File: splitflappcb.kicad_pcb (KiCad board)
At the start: 2 copper layers, 40 x 80 mm, 46 parts, among them J1 Conn_01x04_Pin, J2 Conn_01x04_Pin, J3 Conn_01x05_Pin, J4 AddressJumpers, J5 HallSensor, J6 AVR-ISP-6, J7 Serial-328P, J8 Serial-ESP12E, J9 WS2815, SW1 RESET, U1 TPS5430, U2 ULN2003A, U3 ATmega328P-A, U4 ESP-12E, Y2 16MHz

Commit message: how many attempts does it take
me when i try to use git
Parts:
- removed the REF** at (74.5, 111.3)
- removed the REF** at (82.9, 111.4)
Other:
- board text added: "Split-Flap PCB Erzerum's Mod"
- board text added: "rev 1.2b"
- board text removed: "Split-Flap Fae PCB"
- board text removed: "rev 1.2"

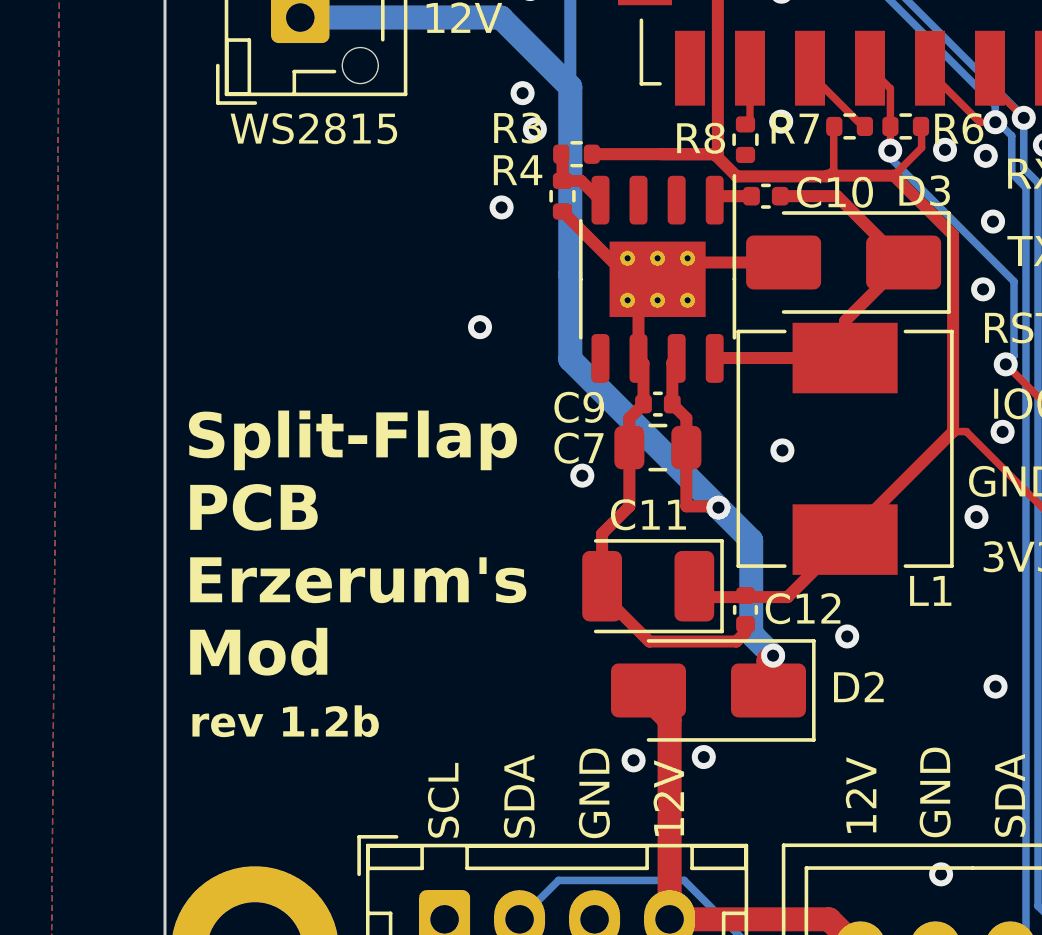
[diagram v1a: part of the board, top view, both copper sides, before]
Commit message: Changed out a tantalum capacitor for four better ones
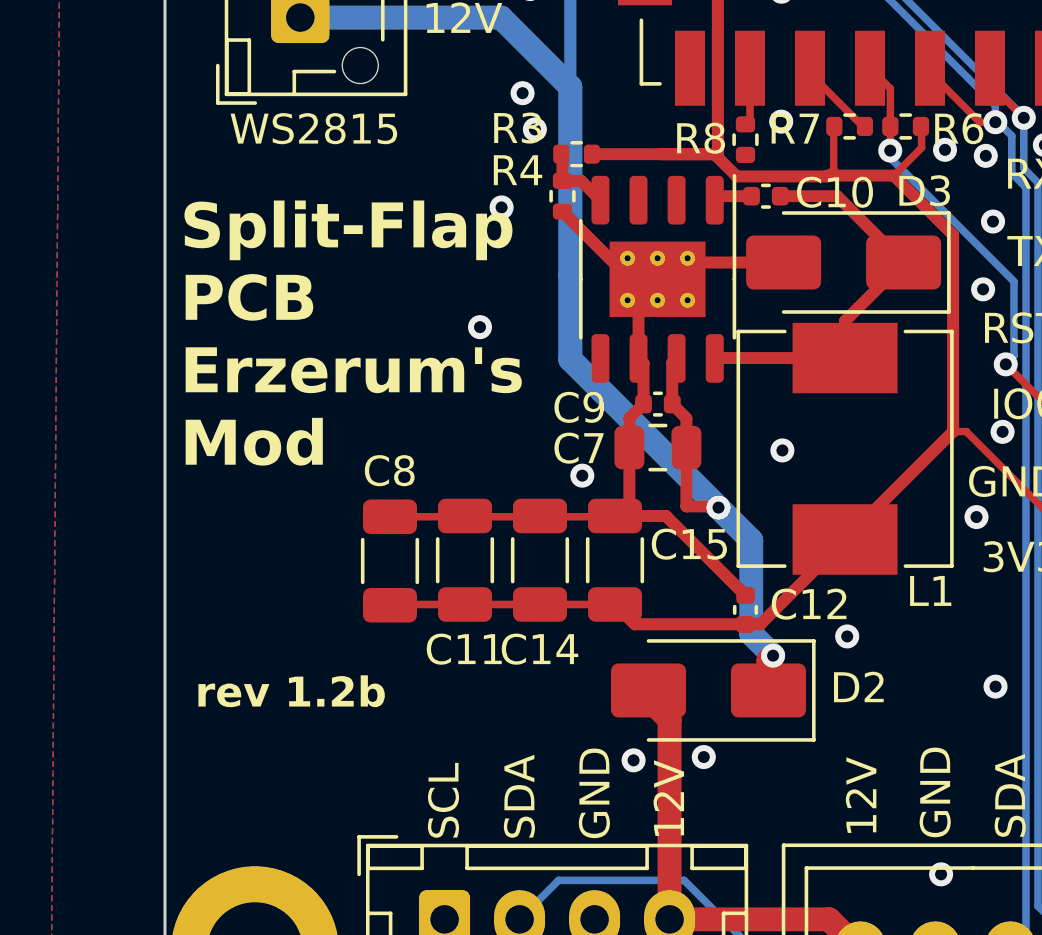
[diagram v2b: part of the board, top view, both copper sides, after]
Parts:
- added C14: 100u, Capacitor_SMD:C_1206_3216Metric, F.Cu at (79.5, 111.0)
- added C15: 100u, Capacitor_SMD:C_1206_3216Metric, F.Cu at (82.0, 111.0)
- added C8: 100u, Capacitor_SMD:C_1206_3216Metric, F.Cu at (74.5, 111.0)
- C11: value 220uF -> 100u; footprint Capacitor_Tantalum_SMD:CP_EIA-3528-21_Kemet-B -> Capacitor_SMD:C_1206_3216Metric
- moved C11 6.17 mm to (77.0, 111.0), turned to 90 degrees
- turned C12 to 90 degrees
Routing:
- net +3V3: track 141.7 -> 152.1 mm
- net GND: track 36.6 -> 41.2 mm

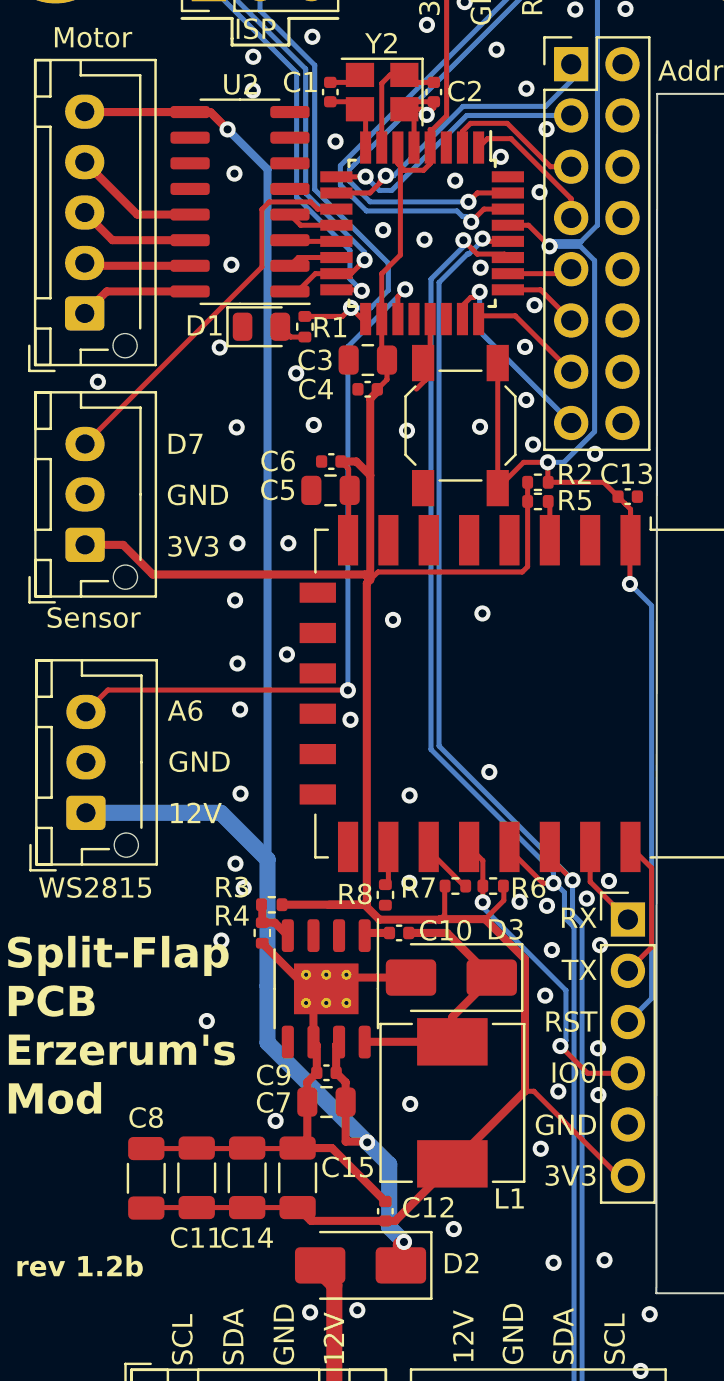
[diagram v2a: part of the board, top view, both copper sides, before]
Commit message: Fixed several drc errors
also slightly adjusted some of the silkscreen
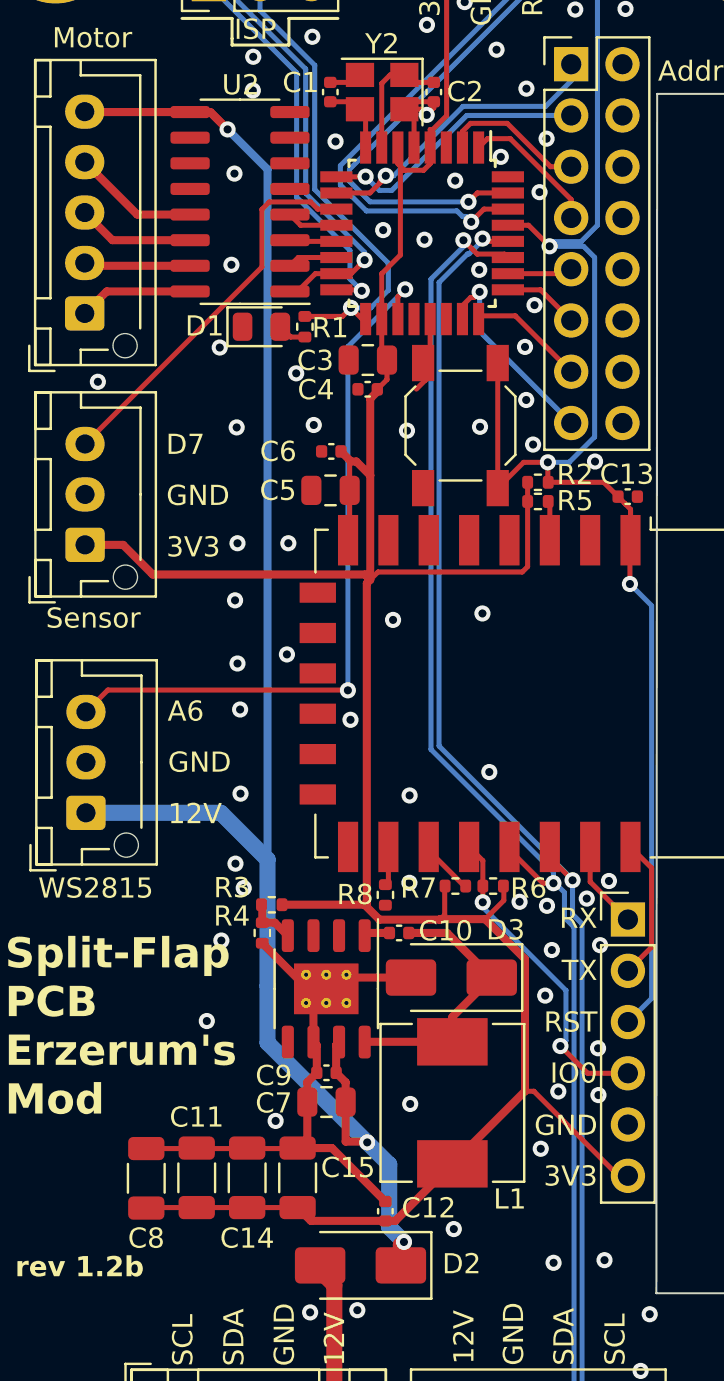
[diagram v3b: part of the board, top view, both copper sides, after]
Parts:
- moved C6 0.50 mm to (83.7, 75.0)
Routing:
- net +3V3: track 152.1 -> 151.1 mm
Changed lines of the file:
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@@
 		(tags "capacitor")
 		(property "Reference" "C8"
-			(at 2.975 0 0)
+			(at -2.975 0 0)
 			(layer "F.SilkS")
 			(effects
@@
 	(footprint "Capacitor_SMD:C_0402_1005Metric"
 		(layer "F.Cu")
-		(at 83.67 75.5)
+		(at 83.67 75)
 		(descr "Capacitor SMD 0402 (1005 Metric), square (rectangular) end terminal, IPC_7351 nominal, (Body size source: IPC-SM-782 page 76, https://www.pcb-3d.com/wordpress/wp-content/uploads/ipc-sm-782a_amendment_1_and_2.pdf), generated with kicad-footprint-generator")
 		(tags "capacitor")
@@
 		(tags "capacitor")
 		(property "Reference" "C11"
-			(at -3 0 0)
+			(at 3 0 0)
 			(layer "F.SilkS")
 			(effects
@@
 	)
 	(segment
+		(start 84.58 79.32)
+		(end 84.58 76.93)
+		(width 0.25)
+		(layer "F.Cu")
+		(net 4)
+	)
+	(segment
 		(start 85.6 81.36)
 		(end 85.6 76.19)
@@
 	)
 	(segment
-		(start 84.53 75.88)
-		(end 84.53 79.37)
-		(width 0.25)
+		(start 84.65 75.5)
+		(end 84.15 75)
+		(width 0.4)
 		(layer "F.Cu")
 		(net 4)
 	)
 	(segment
-		(start 84.18 75.53)
-		(end 84.53 75.88)
-		(width 0.25)
+		(start 85.6 81.36)
+		(end 85.43 81.53)
+		(width 0.4)
 		(layer "F.Cu")
 		(net 4)
@@
 	)
 	(segment
-		(start 85.43 81.53)
-		(end 85.6 81.36)
-		(width 0.4)
+		(start 84.58 76.93)
+		(end 84.58 75.43)
+		(width 0.25)
 		(layer "F.Cu")
 		(net 4)
 	)
 	(segment
-		(start 83.53 97.465)
-		(end 85.43 97.465)
-		(width 0.4)
+		(start 84.5 79.4)
+		(end 84.58 79.32)
+		(width 0.25)
 		(layer "F.Cu")
 		(net 4)
@@
 	)
 	(segment
+		(start 84.58 75.43)
+		(end 84.15 75)
+		(width 0.25)
+		(layer "F.Cu")
+		(net 4)
+	)
+	(segment
 		(start 73.349924 79.63)
 		(end 71.465 79.63)
@@
 	)
 	(segment
-		(start 85.43 97.465)
-		(end 85.43 81.53)
-		(width 0.4)
-		(layer "F.Cu")
-		(net 4)
-	)
-	(segment
 		(start 85.6 81.36)
 		(end 85.985 80.975)
@@
 	)
 	(segment
-		(start 93.71 106.71)
-		(end 97.91 110.91)
-		(width 0.25)
+		(start 84.91 75.5)
+		(end 84.65 75.5)
+		(width 0.4)
 		(layer "F.Cu")
 		(net 4)
 	)
 	(segment
-		(start 84.53 79.37)
-		(end 84.5 79.4)
+		(start 93.71 106.71)
+		(end 97.91 110.91)
 		(width 0.25)
 		(layer "F.Cu")
@@
 	)
 	(segment
+		(start 85.43 81.53)
+		(end 85.43 97.465)
+		(width 0.4)
+		(layer "F.Cu")
+		(net 4)
+	)
+	(segment
 		(start 88.57 60.74)
 		(end 88.57 59.94)
@@
 	)
 	(segment
-		(start 81.23 97.465)
-		(end 85.316262 97.465)
-		(width 0.4)
-		(layer "F.Cu")
-		(net 4)
-	)
-	(segment
-		(start 84.91 75.5)
-		(end 84.15 75.5)
-		(width 0.4)
-		(layer "F.Cu")
-		(net 4)
-	)
-	(segment
 		(start 89.29 96.56)
 		(end 89.29 97.97)
@@
 	)
 	(segment
+		(start 85.43 97.465)
+		(end 81.23 97.465)
+		(width 0.4)
+		(layer "F.Cu")
+		(net 4)
+	)
+	(segment
 		(start 88.700305 59.045)
 		(end 89.385 58.360305)
@@
 	)
 	(segment
-		(start 91.41 59.5)
-		(end 90.97 59.94)
+		(start 92.54 59.5)
+		(end 91.41 59.5)
 		(width 0.25)
 		(layer "F.Cu")
@@
 	)
 	(segment
-		(start 95.56 62.48)
-		(end 92.58 59.5)
+		(start 91.41 59.5)
+		(end 90.97 59.94)
 		(width 0.25)
 		(layer "F.Cu")
@@
 	(segment
 		(start 95.56 63.43)
-		(end 95.56 62.48)
+		(end 95.56 62.52)
 		(width 0.25)
 		(layer "F.Cu")
@@
 	)
 	(segment
-		(start 92.58 59.5)
-		(end 91.41 59.5)
+		(start 95.56 62.52)
+		(end 92.54 59.5)
 		(width 0.25)
 		(layer "F.Cu")
@@
 	)
 	(segment
+		(start 96.72 65.380328)
+		(end 96.72 74.28)
+		(width 0.25)
+		(layer "B.Cu")
+		(net 22)
+	)
+	(segment
 		(start 90.77 51.85)
 		(end 82.69 51.85)
@@
 	)
 	(segment
-		(start 96.72 74.019344)
-		(end 95.199344 75.54)
+		(start 96.72 74.28)
+		(end 95.46 75.54)
 		(width 0.25)
 		(layer "B.Cu")
@@
 	)
 	(segment
-		(start 94.4873 64.8327)
-		(end 96.012044 64.8327)
+		(start 93.61 49.01)
+		(end 90.77 51.85)
 		(width 0.25)
 		(layer "B.Cu")
@@
 	)
 	(segment
-		(start 93.61 49.01)
-		(end 90.77 51.85)
+		(start 95.46 75.54)
+		(end 94.4 75.54)
+		(width 0.25)
+		(layer "B.Cu")
+		(net 22)
+	)
+	(segment
+		(start 96.172372 64.8327)
+		(end 96.72 65.380328)
 		(width 0.25)
 		(layer "B.Cu")
@@
 	)
 	(segment
-		(start 96.012044 64.8327)
-		(end 96.72 65.540656)
-		(width 0.25)
-		(layer "B.Cu")
-		(net 22)
-	)
-	(segment
-		(start 95.199344 75.54)
-		(end 94.4 75.54)
+		(start 94.4873 64.8327)
+		(end 96.172372 64.8327)
 		(width 0.25)
 		(layer "B.Cu")
@@
 	)
 	(segment
-		(start 96.72 65.540656)
-		(end 96.72 74.019344)
-		(width 0.25)
-		(layer "B.Cu")
-		(net 22)
-	)
-	(segment
 		(start 99.545 82.645)
 		(end 98.47 81.57)
@@
 	)
 	(via
-		(at 91.071095 65.8945)
+		(at 91 66)
 		(size 0.8)
 		(drill 0.4)
@@
 	)
 	(via
-		(at 94.34013 59.026812)
+		(at 94.34013 59.5)
 		(size 0.8)
 		(drill 0.4)
@@
 	)
 	(via
-		(at 96.74 75.12)
+		(at 96.74 75.5)
 		(size 0.8)
 		(drill 0.4)

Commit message: ordered rev1
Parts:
- removed D1: LED, LED_SMD:LED_0805_2012Metric
- removed D2, D3: SS54, Diode_SMD:D_SMA
- removed H1, H2, H3, H4: MountingHole_Pad, MountingHole:MountingHole_3.2mm_M3_DIN965_Pad
- removed L1: 47uH, Inductor_SMD:L_Chilisin_BMRx00060630
- removed R1: 220, Resistor_SMD:R_0402_1005Metric
- removed R2, R3, R5, R6, R7, R8: 10k, Resistor_SMD:R_0402_1005Metric
- removed R4: 5k9, Resistor_SMD:R_0402_1005Metric
- removed REF**: KiCad-Logo2_6mm_SilkScreen, Symbol:KiCad-Logo2_6mm_SilkScreen
- removed SW1: RESET, Button_Switch_SMD:SW_SPST_SKQG_WithStem
- removed Y2: 16MHz, Crystal:Crystal_SMD_3225-4Pin_3.2x2.5mm
- added C16: 10u, Capacitor_SMD:C_0603_1608Metric, F.Cu at (287.9, 26.9)
- added C17: 1u, Capacitor_SMD:C_0603_1608Metric, F.Cu at (309.9, 32.9)
- added J10: Conn_01x05_Pin, Connector_JST:JST_XH_B5B-XH-AM_1x05_P2.50mm_Vertical, F.Cu at (196.1, 24.4)
- added J11: HallSensor, Connector_PinHeader_2.54mm:PinHeader_1x03_P2.54mm_Vertical, F.Cu at (240.5, 25.9)
- added J12: Conn_ARM_SWD_TagConnect_TC2030-NL, Connector:Tag-Connect_TC2030-IDC-NL_2x03_P1.27mm_Vertical, F.Cu at (217.3, 26.4)
- added J13: Conn_01x05_Pin, Connector_JST:JST_XH_B5B-XH-AM_1x05_P2.50mm_Vertical, F.Cu at (246.5, 24.4)
- added J14: HallSensor, Connector_PinHeader_2.54mm:PinHeader_1x03_P2.54mm_Vertical, F.Cu at (290.9, 25.9)
- added J15: Conn_01x03_Pin, Connector_PinHeader_2.54mm:PinHeader_1x03_P2.54mm_Vertical, F.Cu at (277.6, 29.6)
- added J16: Conn_01x05_Pin, Connector_JST:JST_XH_B5B-XH-AM_1x05_P2.50mm_Vertical, F.Cu at (296.9, 24.4)
- added J17: Conn_01x04_Pin, Connector_JST:JST_XH_B6B-XH-AM_1x06_P2.50mm_Vertical, F.Cu at (318.4, 39.8)
- added JP1: Jumper_2_Small_Bridged, Jumper:SolderJumper-2_P1.3mm_Bridged_RoundedPad1.0x1.5mm, F.Cu at (183.1, 34.2)
- added JP2: Jumper_2_Small_Open, Jumper:SolderJumper-2_P1.3mm_Open_RoundedPad1.0x1.5mm, F.Cu at (173.4, 26.2)
- added U5: ULN2003A, Package_SO:SOIC-16_3.9x9.9mm_P1.27mm, F.Cu at (202.1, 32.9)
- added U6: ULN2003A, Package_SO:SOIC-16_3.9x9.9mm_P1.27mm, F.Cu at (252.5, 32.9)
- added U7: ULN2003A, Package_SO:SOIC-16_3.9x9.9mm_P1.27mm, F.Cu at (302.9, 32.9)
- C1: value 22pF -> 10u; footprint Capacitor_SMD:C_0402_1005Metric -> Capacitor_SMD:C_0603_1608Metric
- C10, C12, C9: value 100n -> 10u; footprint Capacitor_SMD:C_0402_1005Metric -> Capacitor_SMD:C_0603_1608Metric
- C11, C14, C8: value 100u -> 10u; footprint Capacitor_SMD:C_1206_3216Metric -> Capacitor_SMD:C_0603_1608Metric
- C13, C4, C6: value 100n -> 1u; footprint Capacitor_SMD:C_0402_1005Metric -> Capacitor_SMD:C_0603_1608Metric
- C15: value 100u -> 1u; footprint Capacitor_SMD:C_1206_3216Metric -> Capacitor_SMD:C_0603_1608Metric
- C2: value 22pF -> 1u; footprint Capacitor_SMD:C_0402_1005Metric -> Capacitor_SMD:C_0603_1608Metric
- C3, C5: value 10uF -> 10u; footprint Capacitor_SMD:C_0805_2012Metric -> Capacitor_SMD:C_0603_1608Metric
- C7: value 10uF -> 100n; footprint Capacitor_SMD:C_0805_2012Metric -> Capacitor_SMD:C_0603_1608Metric
- J1: footprint Connector_JST:JST_XH_B4B-XH-AM_1x04_P2.50mm_Vertical -> Connector_JST:JST_XH_B6B-XH-AM_1x06_P2.50mm_Vertical
- J2: value Conn_01x04_Pin -> HallSensor; footprint Connector_JST:JST_XH_B4B-XH-AM_1x04_P2.50mm_Vertical -> Connector_PinHeader_2.54mm:PinHeader_1x03_P2.54mm_Vertical
- J4: value AddressJumpers -> Conn_01x05_Pin; footprint Connector_PinHeader_2.54mm:PinHeader_2x08_P2.54mm_Vertical -> Connector_JST:JST_XH_B5B-XH-AM_1x05_P2.50mm_Vertical
- J5: footprint Connector_JST:JST_XH_B3B-XH-AM_1x03_P2.50mm_Vertical -> Connector_PinHeader_2.54mm:PinHeader_1x03_P2.54mm_Vertical
- J6: value AVR-ISP-6 -> HallSensor; footprint Connector_PinHeader_2.54mm:PinHeader_2x03_P2.54mm_Vertical -> Connector_PinHeader_2.54mm:PinHeader_1x03_P2.54mm_Vertical
- J7: value Serial-328P -> Conn_01x05_Pin; footprint Connector_PinHeader_2.54mm:PinHeader_1x05_P2.54mm_Vertical -> Connector_JST:JST_XH_B5B-XH-AM_1x05_P2.50mm_Vertical
- J8: value Serial-ESP12E -> HallSensor; footprint Connector_PinHeader_2.54mm:PinHeader_1x06_P2.54mm_Vertical -> Connector_PinHeader_2.54mm:PinHeader_1x03_P2.54mm_Vertical
- J9: value WS2815 -> Conn_01x04_Pin; footprint Connector_JST:JST_XH_B3B-XH-AM_1x03_P2.50mm_Vertical -> Connector_PinHeader_2.54mm:PinHeader_1x04_P2.54mm_Vertical
- U1: value TPS5430 -> ULN2003A; footprint Package_SO:SOIC-8-1EP_3.9x4.9mm_P1.27mm_EP2.514x3.2mm_ThermalVias -> Package_SO:SOIC-16_3.9x9.9mm_P1.27mm
- U3: value ATmega328P-A -> ULN2003A; footprint Package_QFP:TQFP-32_7x7mm_P0.8mm -> Package_SO:SOIC-16_3.9x9.9mm_P1.27mm
- U4: value ESP-12E -> STM32F030C8Tx; footprint RF_Module:ESP-12E -> Package_QFP:LQFP-48_7x7mm_P0.5mm
- moved C15 193.9 mm to (259.5, 32.9), turned to -90 degrees
- moved C14 184.2 mm to (241.3, 23.0), turned to 0 degrees
- moved J9 157.0 mm to (212.9, 24.6), turned to 0 degrees
- moved C11 138.5 mm to (187.1, 26.9), turned to -90 degrees
- moved C8 127.8 mm to (173.4, 30.1), turned to 0 degrees
- moved C9 121.3 mm to (179.7, 32.0), turned to 0 degrees
- moved C7 119.6 mm to (173.4, 28.4)
- moved C13 119.3 mm to (209.1, 32.9), turned to -90 degrees
- moved J8 116.8 mm to (190.1, 25.9)
- moved C10 113.6 mm to (180.5, 34.3), turned to -90 degrees
- moved J1 113.2 mm to (24.7, 37.4), turned to 90 degrees
- moved C12 110.2 mm to (167.9, 38.6)
- moved J2 104.1 mm to (38.9, 25.9)
- moved U4 93.8 mm to (174.2, 36.9)
- moved C6 86.0 mm to (158.7, 32.9), turned to -90 degrees
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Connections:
- C1 pad 1: GND -> +3V3
- C1 pad 2: Net-(U3-XTAL2/PB7) -> GND
- C10 pad 1: Net-(D3-K) -> +3V3
- C10 pad 2: Net-(U1-BOOT) -> GND
- C13 pad 1: GND -> +12V
- C13 pad 2: /RESET -> GND
- C15 pad 1: +3V3 -> +12V
- C2 pad 1: GND -> +12V
- C2 pad 2: Net-(U3-XTAL1/PB6) -> GND
- C3 pad 1: GND -> +3V3
- C3 pad 2: +3V3 -> GND
- C4 pad 1: GND -> +12V
- C4 pad 2: +3V3 -> GND
- C5 pad 1: GND -> +3V3
- C5 pad 2: +3V3 -> GND
- C6 pad 1: GND -> +12V
- C6 pad 2: +3V3 -> GND
- C7 pad 1: +12V -> /NRST
- C9 pad 1: +12V -> +3V3
- J1 pad 1: /A5/SCL -> GND
- J1 pad 2: /A4/SDA -> GND
- J1 pad 3: GND -> /DATA_OUT
- J1 pad 4: Net-(D2-A) -> +3V3
- J2 pad 1: /A5/SCL -> +3V3
- J2 pad 2: /A4/SDA -> GND
- J2 pad 3: GND -> /1_H
- J3 pad 1: Net-(J3-Pin_1) -> /stepper1/C4
- J3 pad 2: Net-(J3-Pin_2) -> /stepper1/C3
- J3 pad 3: Net-(J3-Pin_3) -> /stepper1/C2
- J3 pad 4: Net-(J3-Pin_4) -> /stepper1/C1
- J4 pad 1: /D6 -> /stepper2/C4
- J4 pad 2: GND -> /stepper2/C3
- J4 pad 3: /D5 -> /stepper2/C2
- J4 pad 4: GND -> /stepper2/C1
- J4 pad 5: /D4 -> +12V
- J5 pad 3: /D7 -> /2_H
- J6 pad 1: /D12 -> +3V3
- J6 pad 2: +3V3 -> GND
- J6 pad 3: /D13 -> /3_H
- J7 pad 1: /D0 -> /stepper3/C4
- J7 pad 2: /D1 -> /stepper3/C3
- J7 pad 3: /RESET -> /stepper3/C2
- J7 pad 4: GND -> /stepper3/C1
- J7 pad 5: +3V3 -> +12V
- J8 pad 1: /01-RX -> +3V3
- J8 pad 2: /01-TX -> GND
- J8 pad 3: /RESET -> /4_H
- J9 pad 1: +12V -> GND
- J9 pad 2: GND -> /SWDIO
- J9 pad 3: /A6 -> /SWCLK
- U1 pad 1: Net-(U1-BOOT) -> /1_1
- U1 pad 2: unconnected-(U1-NC-Pad2) -> /1_2
- U1 pad 3: unconnected-(U1-NC-Pad3) -> /1_3
- U1 pad 4: Net-(U1-VSNS) -> /1_4
- U1 pad 6: GND -> unconnected-(U1-I6-Pad6)
- U1 pad 7: +12V -> unconnected-(U1-I7-Pad7)
- U1 pad 8: Net-(D3-K) -> GND
- U1 pad 9: GND -> +12V
- U2 pad 1: /D11 -> /2_1
- U2 pad 13: Net-(J3-Pin_4) -> /stepper2/C1
- U2 pad 14: Net-(J3-Pin_3) -> /stepper2/C2
- U2 pad 15: Net-(J3-Pin_2) -> /stepper2/C3
- U2 pad 16: Net-(J3-Pin_1) -> /stepper2/C4
- U2 pad 2: /D10 -> /2_2
- U2 pad 3: /D9 -> /2_3
- U2 pad 4: /D8 -> /2_4
- U3 pad 1: /D3 -> /3_1
- U3 pad 10: /D6 -> unconnected-(U3-O7-Pad10)
- U3 pad 11: /D7 -> unconnected-(U3-O6-Pad11)
- U3 pad 12: /D8 -> unconnected-(U3-O5-Pad12)
- U3 pad 13: /D9 -> /stepper3/C1
- U3 pad 14: /D10 -> /stepper3/C2
- U3 pad 15: /D11 -> /stepper3/C3
- U3 pad 16: /D12 -> /stepper3/C4
- U3 pad 2: /D4 -> /3_2
- U3 pad 3: GND -> /3_3
- U3 pad 4: +3V3 -> /3_4
- U3 pad 5: GND -> unconnected-(U3-I5-Pad5)
- U3 pad 6: +3V3 -> unconnected-(U3-I6-Pad6)
- U3 pad 7: Net-(U3-XTAL1/PB6) -> unconnected-(U3-I7-Pad7)
- U3 pad 8: Net-(U3-XTAL2/PB7) -> GND
- U3 pad 9: /D5 -> +12V
- U4 pad 1: /RESET -> +3V3
- U4 pad 10: unconnected-(U4-MISO-Pad10) -> /3_4
- U4 pad 11: unconnected-(U4-GPIO9-Pad11) -> /3_3
- U4 pad 12: unconnected-(U4-GPIO10-Pad12) -> /3_2
- U4 pad 13: unconnected-(U4-MOSI-Pad13) -> /3_1
- U4 pad 14: unconnected-(U4-SCLK-Pad14) -> /3_H
- U4 pad 15: GND -> /2_4
- U4 pad 16: Net-(U4-GPIO15) -> /2_3
- U4 pad 17: /01-IO2 -> /2_2
- U4 pad 18: /01-IO0 -> /2_1
- U4 pad 19: /A4/SDA -> /2_H
- U4 pad 2: unconnected-(U4-ADC-Pad2) -> /4_4
- U4 pad 20: /A5/SCL -> unconnected-(U4-PB2-Pad20)
- U4 pad 21: /01-RX -> unconnected-(U4-PB10-Pad21)
- U4 pad 22: /01-TX -> unconnected-(U4-PB11-Pad22)
- U4 pad 3: /01-EN -> /4_3
- U4 pad 4: unconnected-(U4-GPIO16-Pad4) -> /4_2
- U4 pad 5: unconnected-(U4-GPIO14-Pad5) -> /4_1
- U4 pad 6: unconnected-(U4-GPIO12-Pad6) -> /4_H
- U4 pad 7: unconnected-(U4-GPIO13-Pad7) -> /NRST
- U4 pad 8: +3V3 -> GND
- U4 pad 9: unconnected-(U4-CS0-Pad9) -> +3V3
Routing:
- net +12V: track 84.9 -> 394.5 mm, vias 3 -> 0
- net +3V3: track 151.1 -> 429.4 mm
- net /DATA_OUT: track 0.00 -> 162.0 mm
- net /DATA_IN: track 0.00 -> 154.5 mm
- net /1_H: track 0.00 -> 140.7 mm
- net /6_4: track 0.00 -> 133.7 mm
- net /6_3: track 0.00 -> 132.2 mm
- net /1_1: track 0.00 -> 131.6 mm
- net /6_2: track 0.00 -> 130.6 mm
- net /1_2: track 0.00 -> 130.2 mm
- net /6_1: track 0.00 -> 129.2 mm
- net /1_3: track 0.00 -> 128.8 mm
- net /6_H: track 0.00 -> 128.8 mm
- net /1_4: track 0.00 -> 126.2 mm
- net /A5/SCL: track 90.8 -> 0.00 mm, vias 2 -> 0
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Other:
- board size 40 x 80 mm -> 302 x 25.4 mm
- board text added: "12v"
- board text added: "3v3"
- board text added: "CJG"
- board text added: "CJK"
- board text added: "D_IN"
- board text added: "D_OUT"
- board text added: "PCB"
- board text added: "arson"
- board text added: "erzerum"
- board text added: "flap"
- board text added: "rev1"
- board text added: "six"
- board text added: "this board was developed in 4 hours"
- board text removed: "12V"
- board text removed: "3V3"
- board text removed: "A2"
- board text removed: "A3"
- board text removed: "A4"
- board text removed: "A5"
- board text removed: "A6"
- board text removed: "Address"
- board text removed: "BOOT"
- board text removed: "D10"
- board text removed: "D11"
- board text removed: "D3"
- board text removed: "D4"
- board text removed: "D5"
- board text removed: "D6"
- board text removed: "D7"
- board text removed: "D8"
- board text removed: "D9"
- board text removed: "IO0"
- board text removed: "ISP"
- board text removed: "MISO"
- board text removed: "MOSI"
- board text removed: "Motor"
- board text removed: "RST"
- board text removed: "RX"
- board text removed: "SCK"
- board text removed: "SCL"
- board text removed: "SDA"
- board text removed: "Sensor"
- board text removed: "Split-Flap PCB Erzerum's Mod"
- board text removed: "TX"
- board text removed: "WS2815"
- board text removed: "rev 1.2b"
